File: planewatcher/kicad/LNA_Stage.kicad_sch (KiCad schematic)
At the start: 8 parts, among them U7 TQP3M9036

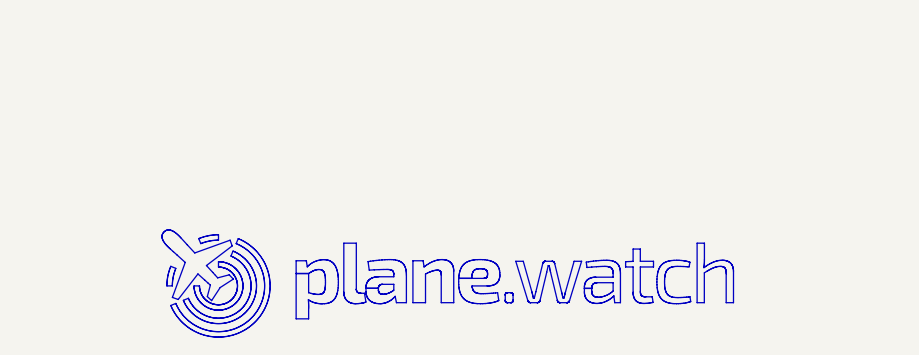
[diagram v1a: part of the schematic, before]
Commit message: add license & copyright info to schematic and pcb. fix layer window.
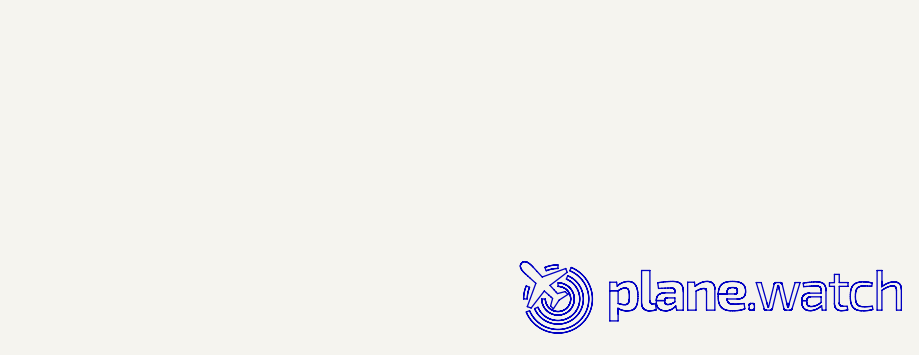
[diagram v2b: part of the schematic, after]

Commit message: added lcsc_ids to all parts
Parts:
- C28: lcsc_id (none) -> C528974
- C29: lcsc_id (none) -> C161163
- C30: lcsc_id (none) -> C161523
- C31, C32, C33: lcsc_id (none) -> C2941926
- L7: MPN 0603CS-68NXJLU -> 0603CS-68NXJLW; lcsc_id (none) -> C19191685
- U7: lcsc_id (none) -> C920261
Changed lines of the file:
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@@
+			)
+		)
+		(property "lcsc_id" "C528974"
+			(at 167.64 45.72 0)
+			(hide yes)
+			(show_name no)
+			(do_not_autoplace no)
+			(effects
+				(font
+					(size 1.27 1.27)
+				)
 			)
 		)
@@
 			)
 		)
+		(property "lcsc_id" "C2941926"
+			(at 120.65 104.14 0)
+			(hide yes)
+			(show_name no)
+			(do_not_autoplace no)
+			(effects
+				(font
+					(size 1.27 1.27)
+				)
+			)
+		)
 		(pin "2"
 		)
@@
 			)
 		)
+		(property "lcsc_id" "C2941926"
+			(at 167.64 104.14 0)
+			(hide yes)
+			(show_name no)
+			(do_not_autoplace no)
+			(effects
+				(font
+					(size 1.27 1.27)
+				)
+			)
+		)
 		(pin "2"
 		)
@@
 			)
 		)
+		(property "lcsc_id" "C161163"
+			(at 167.64 58.42 0)
+			(hide yes)
+			(show_name no)
+			(do_not_autoplace no)
+			(effects
+				(font
+					(size 1.27 1.27)
+				)
+			)
+		)
 		(pin "1"
 		)
@@
 			)
 		)
+		(property "lcsc_id" "C161523"
+			(at 167.64 71.12 0)
+			(hide yes)
+			(show_name no)
+			(do_not_autoplace no)
+			(effects
+				(font
+					(size 1.27 1.27)
+				)
+			)
+		)
 		(pin "2"
 		)
@@
 			)
 		)
+		(property "lcsc_id" "C920261"
+			(at 138.43 100.33 0)
+			(hide yes)
+			(show_name no)
+			(do_not_autoplace no)
+			(effects
+				(font
+					(size 1.27 1.27)
+				)
+			)
+		)
 		(pin "6"
 		)
@@
 			)
 		)
+		(property "lcsc_id" "C2941926"
+			(at 167.64 83.82 0)
+			(hide yes)
+			(show_name no)
+			(do_not_autoplace no)
+			(effects
+				(font
+					(size 1.27 1.27)
+				)
+			)
+		)
 		(pin "2"
 		)
@@
 			)
 		)
-		(property "MPN" "0603CS-68NXJLU"
+		(property "MPN" "0603CS-68NXJLW"
 			(at 153.67 93.98 0)
 			(hide yes)
@@
 			(at 153.67 93.98 0)
 			(hide yes)
+			(show_name no)
+			(do_not_autoplace no)
+			(effects
+				(font
+					(size 1.27 1.27)
+				)
+			)
+		)
+		(property "lcsc_id" "C19191685"
+			(at 153.67 93.98 0)
+			(hide yes)

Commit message: update BoM to available parts from LCSC
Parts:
- C30: MPN GRM1555C1H102FA01D -> GCM1555C1H102FA16D; lcsc_id C161523 -> C126493
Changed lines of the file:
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@@
 			)
 		)
-		(property "MPN" "GRM1555C1H102FA01D"
+		(property "MPN" "GCM1555C1H102FA16D"
 			(at 167.64 71.12 0)
 			(hide yes)
@@
 			)
 		)
-		(property "lcsc_id" "C161523"
+		(property "lcsc_id" "C126493"
 			(at 167.64 71.12 0)
 			(hide yes)
